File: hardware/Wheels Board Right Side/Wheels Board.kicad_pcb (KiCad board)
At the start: 2 copper layers, 92.9 x 69.7 mm, 46 parts, among them J1 Conn_01x05, J10 gnd, J11 hall_out, J12 Conn_01x05, J2 24v, J3 Conn_01x03, J4 53307-2471, J6 Conn_01x05_Pin, J7 Conn_01x07, J8 24v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

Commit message: added right side
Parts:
- removed LOGO1: LHRS, UTSVT_Logos:LHRs_LOGO
- moved J6 181.2 mm to (246.2, 69.9)
- moved J10 156.4 mm to (223.4, 100.8), turned to 180 degrees
- moved R9 145.0 mm to (220.4, 73.9)
- moved R2 144.2 mm to (230.6, 69.9), turned to 0 degrees
- moved C7 143.4 mm to (221.7, 70.5)
- moved D6 143.4 mm to (229.4, 77.7)
- moved C9 143.4 mm to (227.6, 78.0)
- moved C5 143.4 mm to (224.8, 70.7)
- moved C6 143.4 mm to (226.4, 70.7)
- moved C8 143.4 mm to (220.4, 77.4)
- moved D3 143.4 mm to (228.9, 71.5)
- moved L1 143.4 mm to (225.2, 86.2)
- moved U4 143.4 mm to (224.0, 76.1)
- moved R10 143.4 mm to (223.2, 70.7)
- moved C10 143.2 mm to (217.0, 85.6)
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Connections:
- J1 pad 1: /ESP_SPI_SS -> /ESP_SPI_MOSI
- J1 pad 2: /ESP_SPI_CLK -> /ESP_SPI_MISO
- J1 pad 3: /ESP_SPI_MISO -> /ESP_SPI_CLK
- J1 pad 4: /ESP_SPI_MOSI -> /ESP_SPI_SS
- J7 pad 2: /IMU_INT1 -> /IMU_INT2
- J7 pad 3: /IMU_INT2 -> /IMU_SPI_MISO
- J7 pad 4: /IMU_SPI_MISO -> /IMU_SPI_MOSI
- J7 pad 5: /IMU_SPI_MOSI -> /IMU_SPI_CLK
- J7 pad 6: /IMU_SPI_CLK -> /IMU_SPI_SS
- J7 pad 7: /IMU_SPI_SS -> /IMU_INT1
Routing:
- net Net-(J3-Pin_2): track 58.9 -> 93.9 mm, vias 0 -> 2
- net /HALL_PSOM: track 54.1 -> 20.0 mm
- net /ESP_SPI_SS: track 48.4 -> 72.4 mm, vias 1 -> 0
- net /HALL_OUT: track 20.4 -> 43.3 mm, vias 0 -> 1
- net +3.3V: track 76.2 -> 53.4 mm, vias 4 -> 3
- net /ESP_UART_TX: track 47.7 -> 67.0 mm, vias 2 -> 3
- net /ESP_UART_RX: track 68.5 -> 86.7 mm, vias 2 -> 3
- net /IMU_INT2: track 43.2 -> 59.9 mm, vias 0 -> 2
- net /IMU_INT1: track 56.0 -> 40.1 mm, vias 4 -> 2
- net /CAN_L: track 87.3 -> 75.1 mm, vias 2 -> 1
- net /IMU_SPI_MISO: track 60.8 -> 54.3 mm, vias 4 -> 2
- net /ESP_SPI_MISO: track 84.1 -> 90.2 mm
- net GND: track 0.39 -> 6.20 mm, vias 49 -> 38
- net /EXTRA_GPIO2: track 32.7 -> 28.8 mm, vias 1 -> 0
- net /CAN_H: track 83.9 -> 80.9 mm, vias 2 -> 1
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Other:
- outline, holes or cut-outs redrawn
- board text added: "GPIO1"
- board text added: "GPIO2"

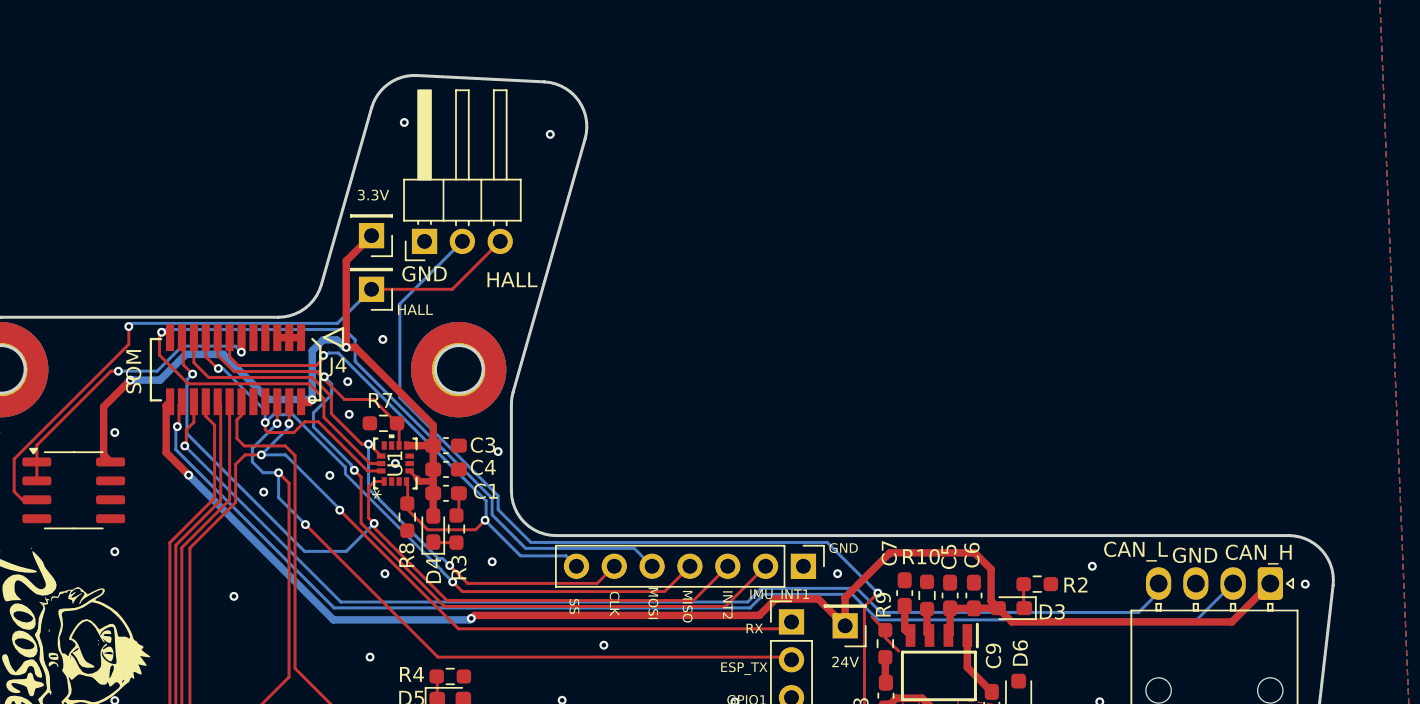
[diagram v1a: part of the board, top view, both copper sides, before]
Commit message: changed hall conn, silkscreen fix
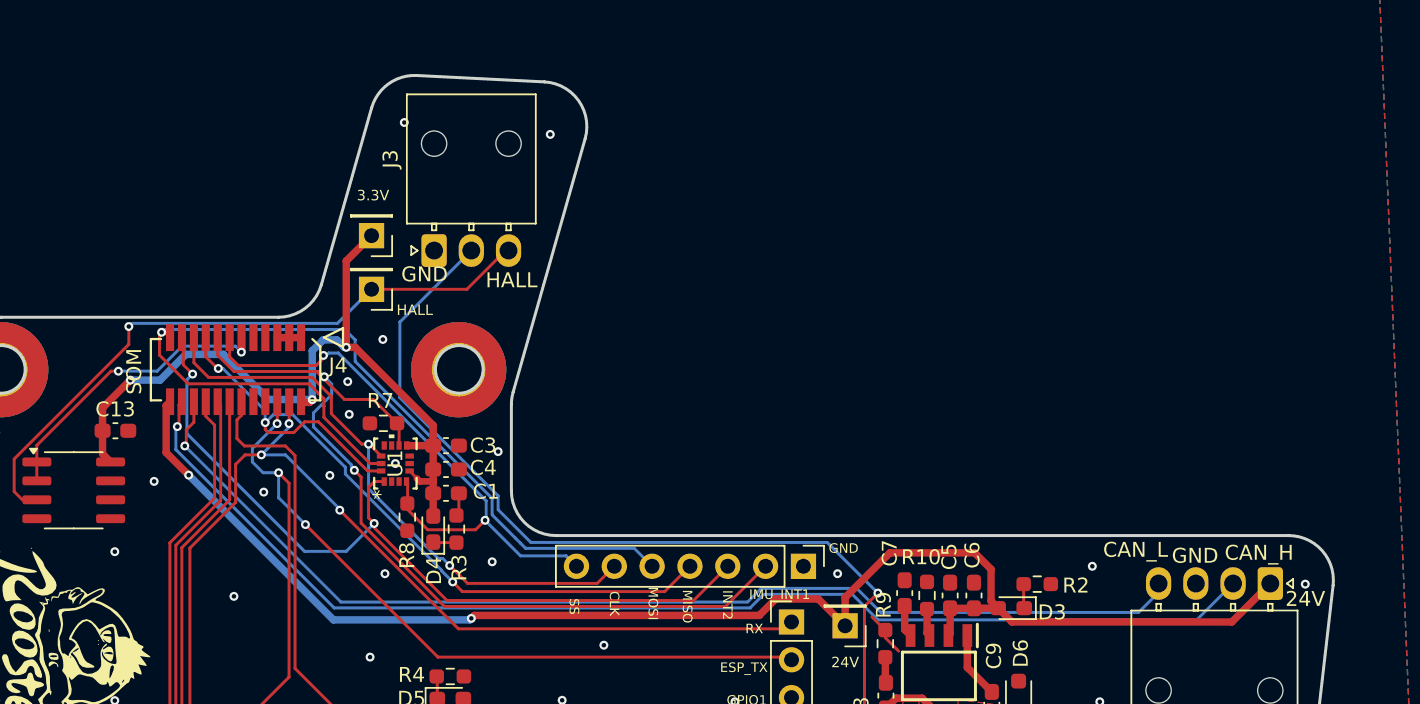
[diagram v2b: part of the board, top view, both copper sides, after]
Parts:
- added C13: 1uf, Capacitor_SMD:C_0603_1608Metric_Pad1.08x0.95mm_HandSolder, F.Cu at (168.7, 59.6)
- J3: footprint Connector_PinHeader_2.54mm:PinHeader_1x03_P2.54mm_Horizontal -> Connector_Molex:Molex_Nano-Fit_105313-xx03_1x03_P2.50mm_Horizontal
- moved J3 0.89 mm to (190.1, 47.5)
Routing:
- net /HALL_OUT: track 43.3 -> 43.9 mm
